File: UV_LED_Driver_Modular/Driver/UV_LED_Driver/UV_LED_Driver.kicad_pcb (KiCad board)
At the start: 2 copper layers, 68.6 x 30.5 mm, 11 parts, among them J1 Conn_02x06_Odd_Even, Q1 IPP80N03S4L-03

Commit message: docs update
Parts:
- removed the REF** at (125.7, 85.1)
- removed the REF** at (125.7, 62.2)
- removed the REF** at (186.7, 62.2)
- removed the REF** at (186.7, 85.1)
- removed the REF** at (142.2, 81.3)
- removed the REF** at (142.2, 66.0)
- added C1: 1uF, Capacitor_SMD:C_1206_3216Metric_Pad1.42x1.75mm_HandSolder, F.Cu at (148.7, 78.1)
- added C2: 100nF, Capacitor_SMD:C_1206_3216Metric_Pad1.42x1.75mm_HandSolder, F.Cu at (157.5, 80.0)
- added J2: Conn_02x05_Odd_Even, Connector_PinHeader_2.54mm:PinHeader_2x05_P2.54mm_Vertical, B.Cu at (172.0, 74.2)
- added R1: 1K, Resistor_SMD:R_1206_3216Metric_Pad1.42x1.75mm_HandSolder, F.Cu at (164.6, 78.7)
- added R4: 1R, Resistor_SMD:R_1206_3216Metric_Pad1.42x1.75mm_HandSolder, F.Cu at (164.6, 82.8)
- added REF**: MountingHole_3.2mm_M3, MountingHole:MountingHole_3.2mm_M3, F.Cu at (193.0, 63.0)
- added REF**: MountingHole_3.2mm_M3, MountingHole:MountingHole_3.2mm_M3, F.Cu at (193.0, 85.2)
- added REF**: MountingHole_3.2mm_M3, MountingHole:MountingHole_3.2mm_M3, F.Cu at (156.1, 74.3)
- added U1: MCP1416, Package_TO_SOT_SMD:SOT-23-5, F.Cu at (154.9, 83.7)
- D1: footprint Connector_Molex_MiniFitJnrExtra:Molex_Mini-Fit_Jr_5569-06A2_2x03_P4.20mm_Horizontal -> Connector_Molex:Molex_Mini-Fit_Jr_5569-02A2_2x01_P4.20mm_Horizontal
- J1: value Conn_02x06_Odd_Even -> Conn_02x08_Odd_Even; footprint Connector_IDC:IDC-Header_2x06_P2.54mm_Vertical -> Connector_PinHeader_2.54mm:PinHeader_2x08_P2.54mm_Vertical
- Q1: value IPP80N03S4L-03 -> NTD60N02R; footprint Package_TO_SOT_THT:TO-220-3_Vertical -> Package_TO_SOT_SMD:TO-252-3_TabPin2; moved to F.Cu
- R3: value R100 -> 1R; footprint Package_TO_SOT_THT:TO-220-2_Vertical -> Resistor_SMD:R_1206_3216Metric_Pad1.42x1.75mm_HandSolder; moved to F.Cu
- moved Q1 30.5 mm to (173.2, 84.5), turned to 0 degrees
- moved R2 24.9 mm to (148.7, 85.7), turned to 270 degrees
- moved J1 19.5 mm to (168.8, 66.5)
- moved R3 15.7 mm to (164.6, 86.7), turned to 180 degrees
- moved D1 13.1 mm to (181.7, 73.9)
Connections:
- D1 pad 2: /UV_LED_DRIVER_MODULE/LED_ANODE_OUT -> VPP
- J1 pad 1: +5V -> /LED_PWM_OUT3
- J1 pad 10: GNDS -> VPP
- J1 pad 11: /UV_PWM -> VPP
- J1 pad 12: Net-(J1-Pad12) -> GNDS
- J1 pad 2: +5V -> /LED_PWM_OUT2
- J1 pad 3: +5V -> /LED_PWM_OUT4
- J1 pad 4: +5V -> /LED_PWM_OUT1
- J1 pad 5: +5V -> /LED_PWM_OUT5
- J1 pad 6: GNDS -> Net-(J1-Pad6)
- J1 pad 7: GNDS -> VPP
- J1 pad 8: GNDS -> VPP
- J1 pad 9: GNDS -> VPP
- Q1 pad 1: /UV_PWM -> Net-(Q1-Pad1)
- Q1 pad 3: GNDS -> Net-(Q1-Pad3)
- R3 pad 1: /UV_LED_DRIVER_MODULE/+5V -> Net-(Q1-Pad3)
- R3 pad 2: /UV_LED_DRIVER_MODULE/LED_ANODE_OUT -> GNDS
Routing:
- net VPP: track 0.00 -> 89.0 mm
- net /UV_LED_DRIVER_MODULE/LED_CATHODE_OUT: track 80.0 -> 11.7 mm, vias 0 -> 19
- net /UV_LED_DRIVER_MODULE/LED_ANODE_OUT: track 64.4 -> 0.00 mm
- net /LED_PWM_OUT1: track 0.00 -> 17.9 mm
- net +5V: track 12.7 -> 0.00 mm
- net /LED_PWM_OUT2: track 0.00 -> 11.0 mm
- net Net-(C2-Pad1): track 0.00 -> 10.4 mm
- net Net-(Q1-Pad3): track 0.00 -> 6.89 mm
- net /UV_PWM: track 34.2 -> 40.1 mm
- net /LED_PWM_OUT5: track 0.00 -> 5.87 mm
- net /LED_PWM_OUT4: track 0.00 -> 5.87 mm
- net /LED_PWM_OUT3: track 0.00 -> 5.87 mm
- net Net-(Q1-Pad1): track 0.00 -> 5.27 mm
- net GNDS: track 25.2 -> 29.8 mm, vias 3 -> 5
- added copper zone on B.Cu, net /UV_LED_DRIVER_MODULE/LED_CATHODE_OUT
- added copper zone on F.Cu, net /UV_LED_DRIVER_MODULE/LED_CATHODE_OUT
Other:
- board size 68.6 x 30.5 mm -> 49.3 x 29.5 mm
- board text added: "1"
- board text added: "2"
- board text added: "3"
- board text added: "4"
- board text added: "5"

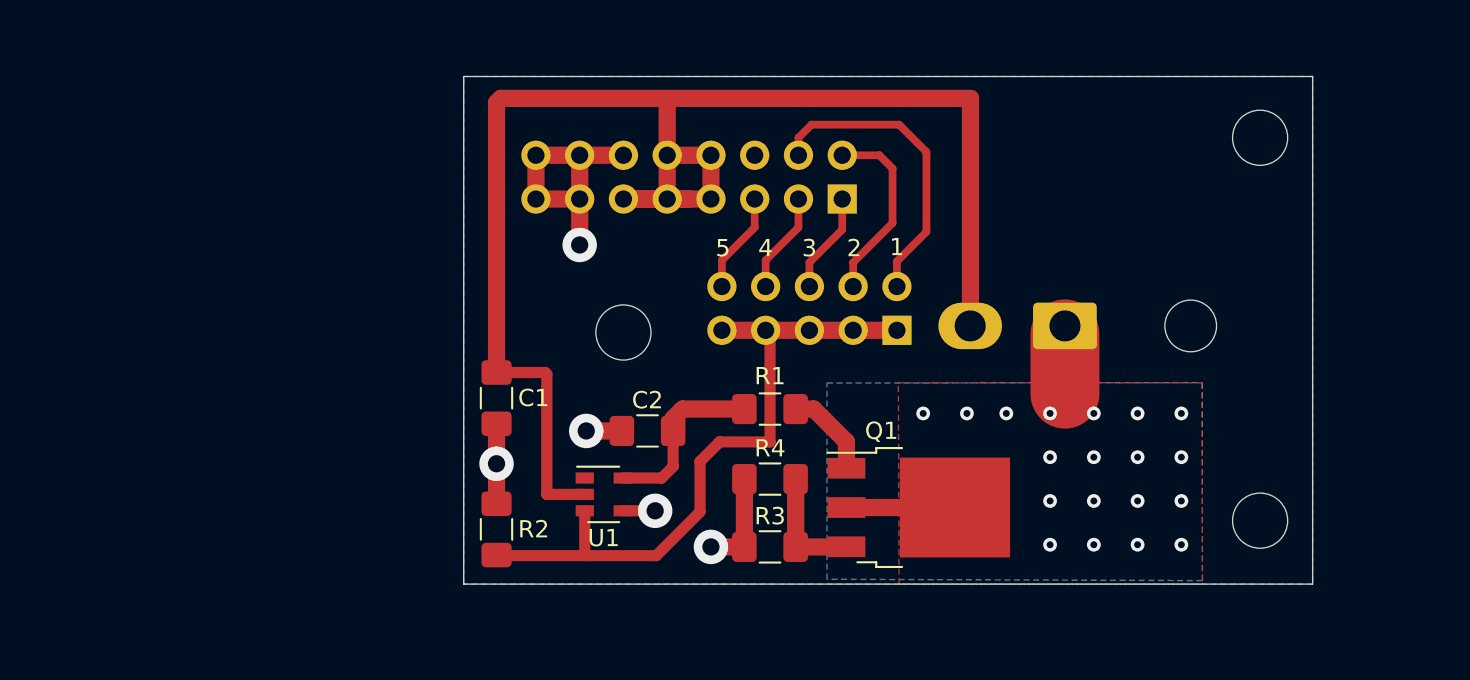
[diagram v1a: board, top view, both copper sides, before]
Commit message: hw update
modified output pin header
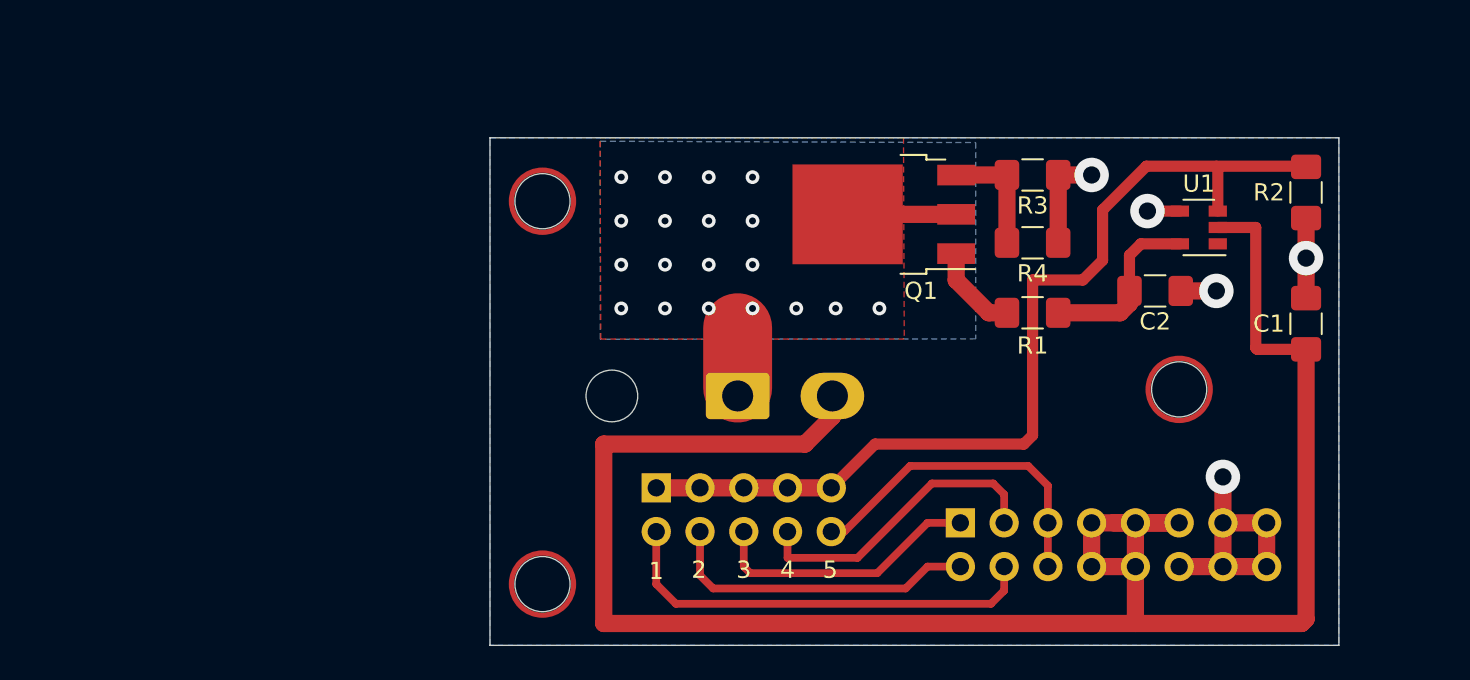
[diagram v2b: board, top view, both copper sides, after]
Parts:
- moved R2 50.9 mm to (195.7, 66.2), turned to 90 degrees
- moved REF** 49.1 mm to (151.4, 88.9), turned to 180 degrees
- moved C1 47.2 mm to (195.7, 73.8), turned to 90 degrees
- moved REF** 45.6 mm to (151.4, 66.7), turned to 180 degrees
- moved U1 37.9 mm to (189.5, 68.2), turned to 180 degrees
- moved REF** 32.4 mm to (188.3, 77.6), turned to 180 degrees
- moved C2 30.6 mm to (186.9, 71.9), turned to 0 degrees
- moved R3 26.4 mm to (179.8, 65.2), turned to 0 degrees
- moved R4 20.5 mm to (179.8, 69.1), turned to 0 degrees
- moved J1 20.0 mm to (175.6, 85.3), turned to 270 degrees
- moved D1 19.4 mm to (162.7, 78.0), turned to 270 degrees
- moved Q1 17.1 mm to (171.2, 67.4), turned to 180 degrees
- moved J2 16.7 mm to (158.0, 83.3), turned to 270 degrees
- moved R1 16.2 mm to (179.8, 73.2), turned to 0 degrees
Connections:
- J1 pad 6: Net-(J1-Pad6) -> /LED_PWM_OUT5
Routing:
- net VPP: track 89.0 -> 114.5 mm
- net /UV_PWM: track 40.1 -> 55.5 mm
- net /LED_PWM_OUT5: track 5.87 -> 19.3 mm
- net /LED_PWM_OUT4: track 5.87 -> 17.8 mm
- net /LED_PWM_OUT3: track 5.87 -> 16.0 mm
- net /LED_PWM_OUT1: track 17.9 -> 25.4 mm
- net /LED_PWM_OUT2: track 11.0 -> 18.5 mm

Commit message: Updated prototype designs for fab
updated readme
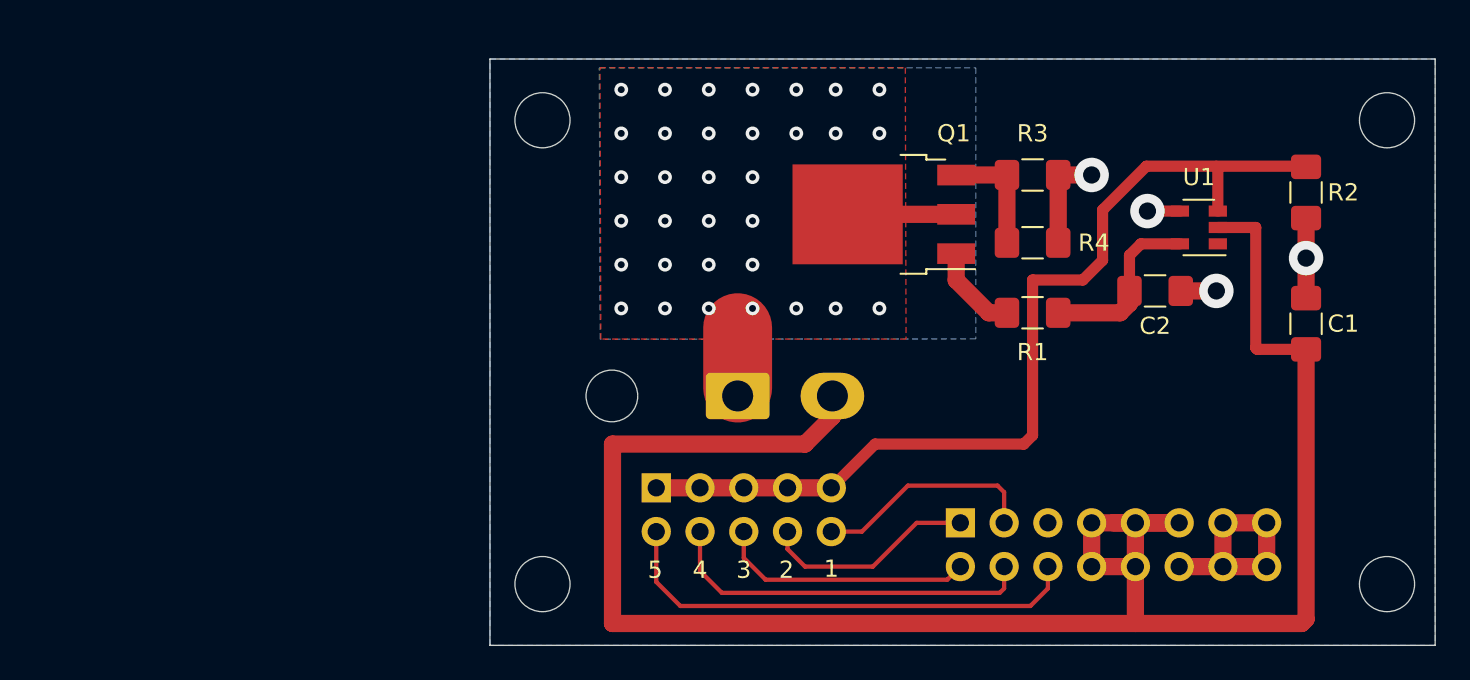
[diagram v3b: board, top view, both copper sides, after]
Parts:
- added REF**: MountingHole_3.2mm_M3, MountingHole:MountingHole_3.2mm_M3, F.Cu at (200.4, 88.9)
- moved REF** 19.7 mm to (200.4, 62.0)
- moved REF** 4.70 mm to (151.4, 62.0)
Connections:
- J1 pad 1: /LED_PWM_OUT3 -> /LED_PWM_OUT2
- J1 pad 2: /LED_PWM_OUT2 -> /LED_PWM_OUT3
- J1 pad 3: /LED_PWM_OUT4 -> /LED_PWM_OUT1
- J1 pad 4: /LED_PWM_OUT1 -> /LED_PWM_OUT4
- J1 pad 5: /LED_PWM_OUT5 -> Net-(J1-Pad5)
- J2 pad 10: /LED_PWM_OUT5 -> /LED_PWM_OUT1
- J2 pad 2: /LED_PWM_OUT1 -> /LED_PWM_OUT5
- J2 pad 4: /LED_PWM_OUT2 -> /LED_PWM_OUT4
- J2 pad 8: /LED_PWM_OUT4 -> /LED_PWM_OUT2
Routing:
- net /LED_PWM_OUT1: track 25.4 -> 13.1 mm
- net /LED_PWM_OUT5: track 19.3 -> 27.9 mm
- net /LED_PWM_OUT2: track 18.5 -> 12.5 mm
- net /LED_PWM_OUT4: track 17.8 -> 21.8 mm
- net GNDS: track 29.8 -> 27.2 mm, vias 5 -> 4
- net /LED_PWM_OUT3: track 16.0 -> 14.9 mm
- net VPP: track 114.5 -> 113.5 mm
- net /UV_LED_DRIVER_MODULE/LED_CATHODE_OUT: vias 19 -> 33
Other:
- board size 49.3 x 29.5 mm -> 54.9 x 34 mm
- board text added: "2 1 VPP GND"
- board text added: "3 4 5 VPP GND"
- board text added: "LED DRIVER RevA 0620"
- board text added: "SIGNAL/PWR BUS"
